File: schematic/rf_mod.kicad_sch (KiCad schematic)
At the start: 31 parts, among them J4A Conn_01x08, Q3 2N3906, Q6 2N3906, U23 4066

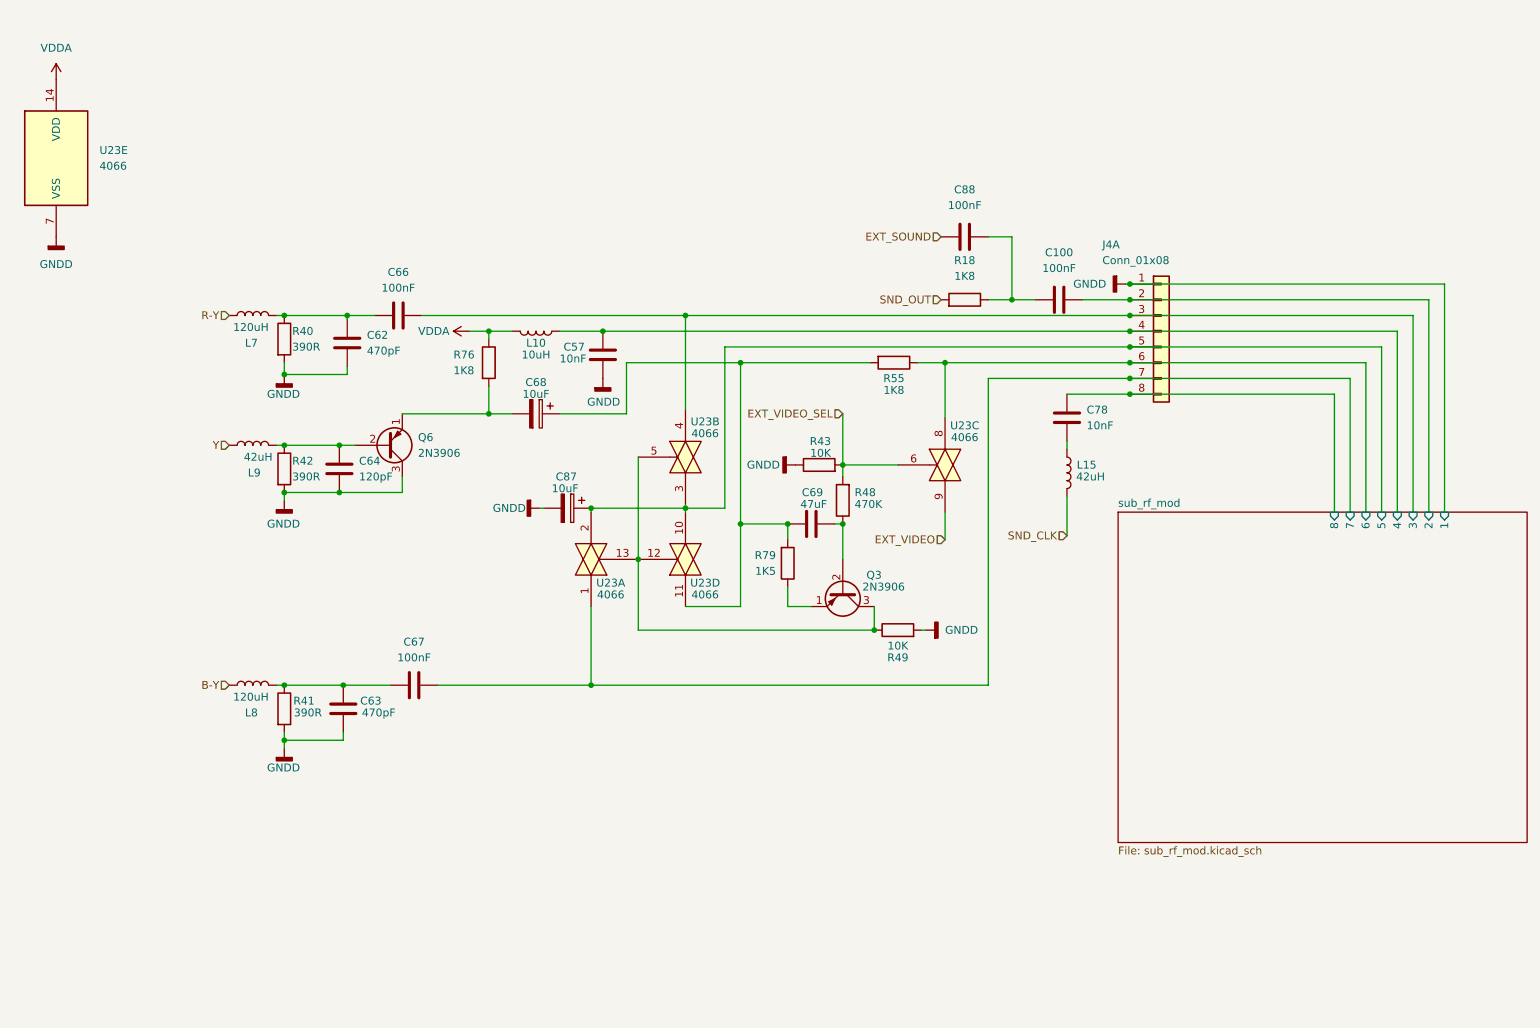
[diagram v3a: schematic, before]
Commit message: adjusted size of the sheets. added pcb version to the rev field. F.0... the 0 is for future fixes on my end. RF PCB is E.0.
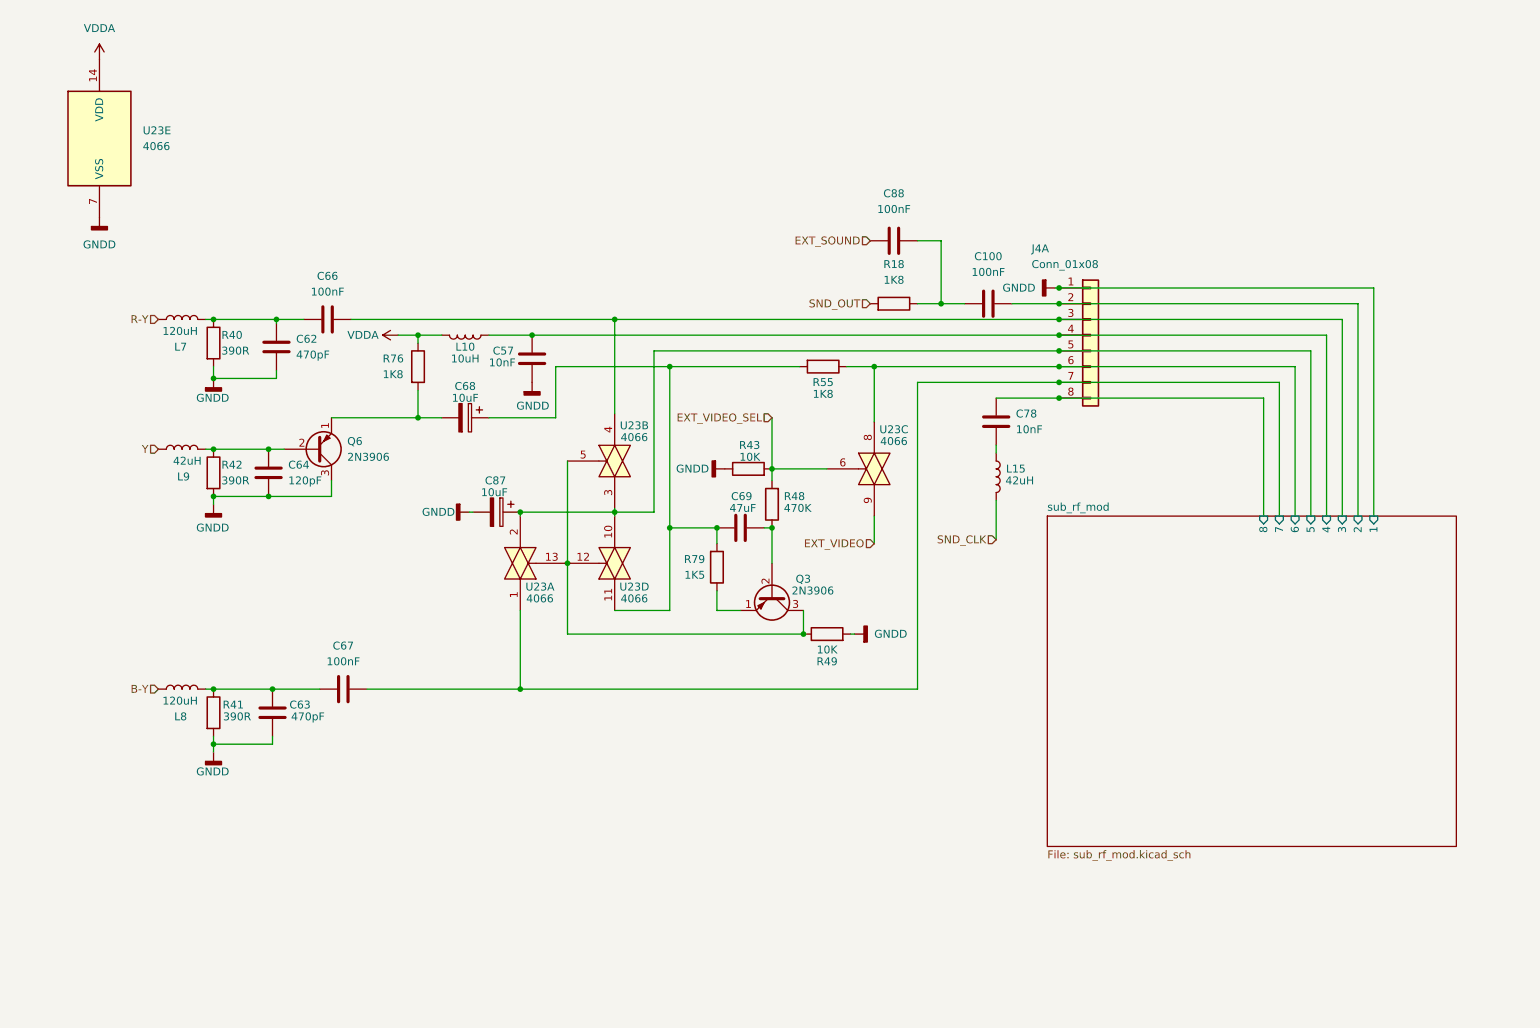
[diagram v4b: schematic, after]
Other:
- title: (none) -> Colecovision Schematic
- moved on the sheet: C100, C57, C62, C63, C64, C66, C67, C68, C69, C78, C87, C88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

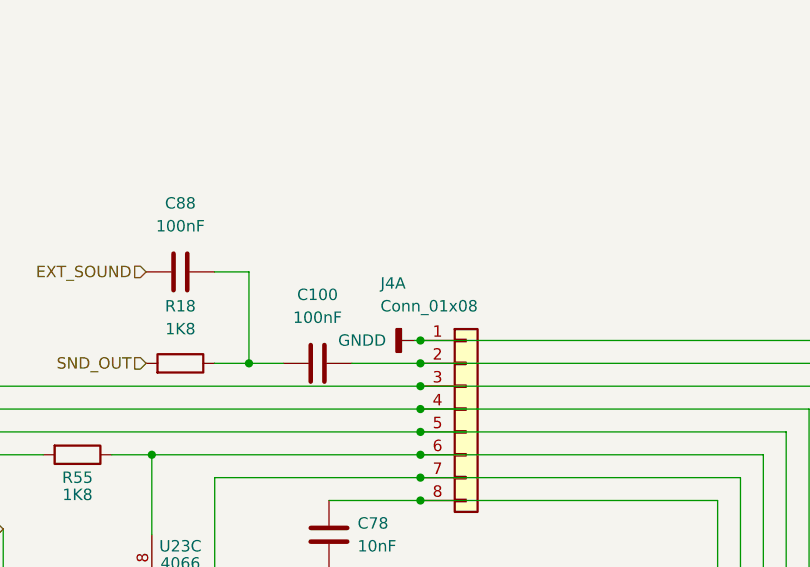
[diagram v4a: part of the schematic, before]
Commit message: cleanup, and started associating components
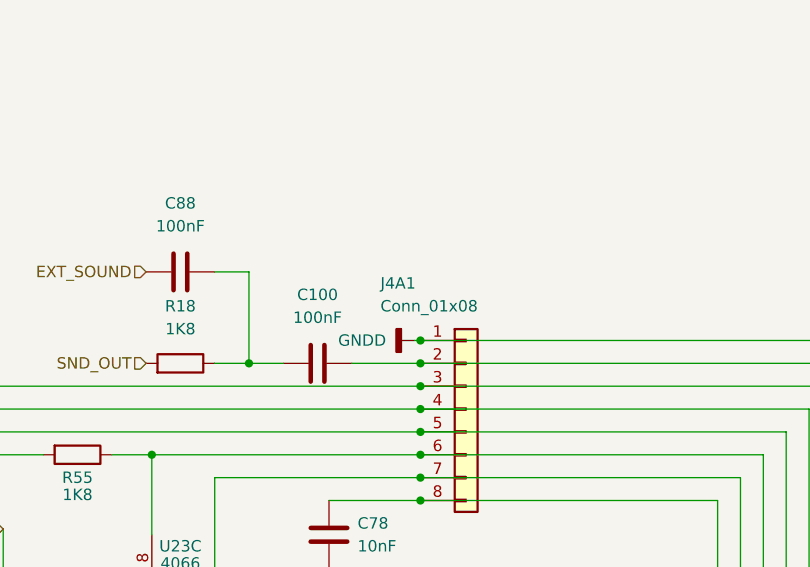
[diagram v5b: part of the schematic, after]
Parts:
- C100, C57, C66, C67, C78, C88: footprint (none) -> Capacitor_THT:C_Disc_D10.0mm_W2.5mm_P5.00mm
- C62, C63, C64: footprint (none) -> Capacitor_THT:C_Disc_D7.0mm_W2.5mm_P5.00mm
- C68, C69, C87: footprint (none) -> Capacitor_THT:CP_Radial_D5.0mm_P2.00mm
- J4A1: renamed from J4A; footprint (none) -> Connector_PinHeader_2.54mm:PinHeader_1x08_P2.54mm_Vertical
- L10, L15, L7, L8, L9: footprint (none) -> Inductor_THT:L_Axial_L12.8mm_D5.8mm_P7.62mm_Vertical_Fastron_HBCC
- Q3, Q6: footprint Package_TO_SOT_THT:TO-92_Inline -> Package_TO_SOT_THT:TO-92_Wide
- R18, R40, R41, R42, R43, R48, R49, R55, R76, R79: footprint (none) -> Resistor_THT:R_Axial_DIN0207_L6.3mm_D2.5mm_P7.62mm_Horizontal
- U23: footprint (none) -> Package_DIP:DIP-14_W7.62mm_LongPads

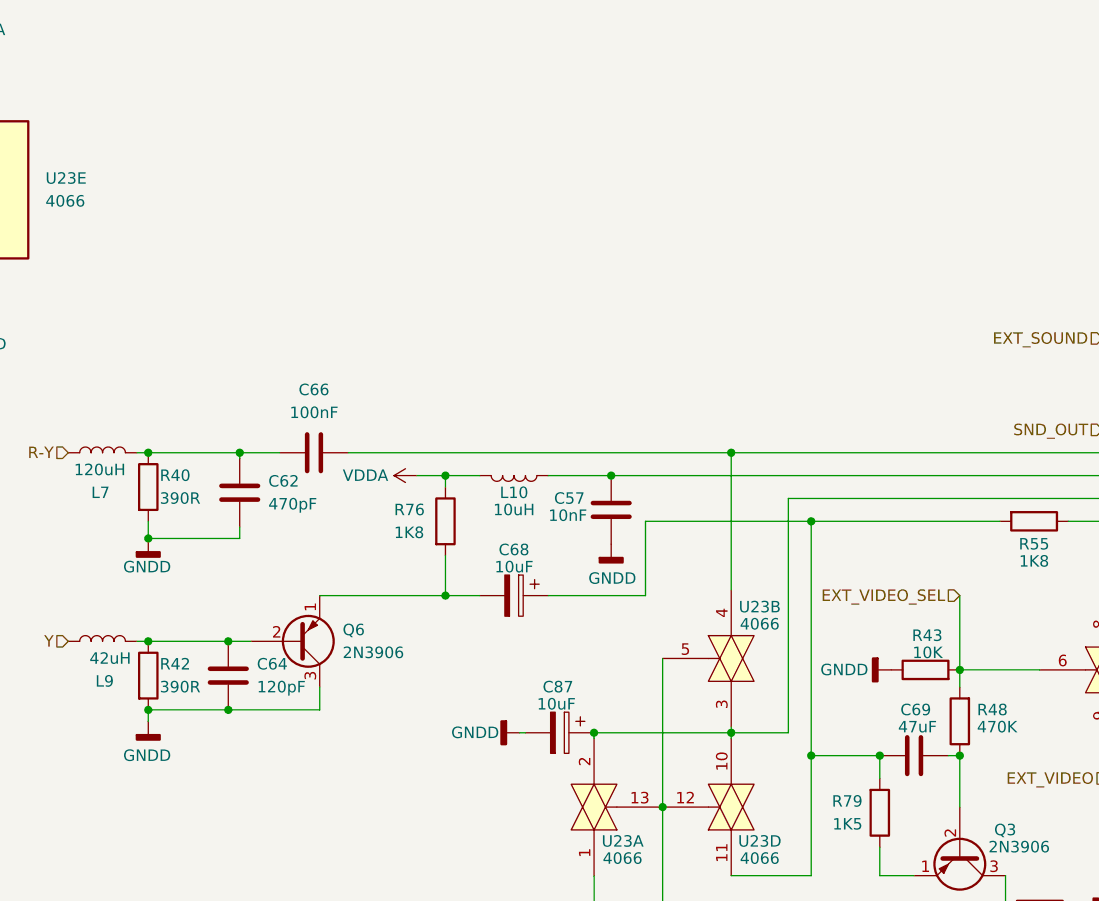
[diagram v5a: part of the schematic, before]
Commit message: first draft of board with components added, no traces
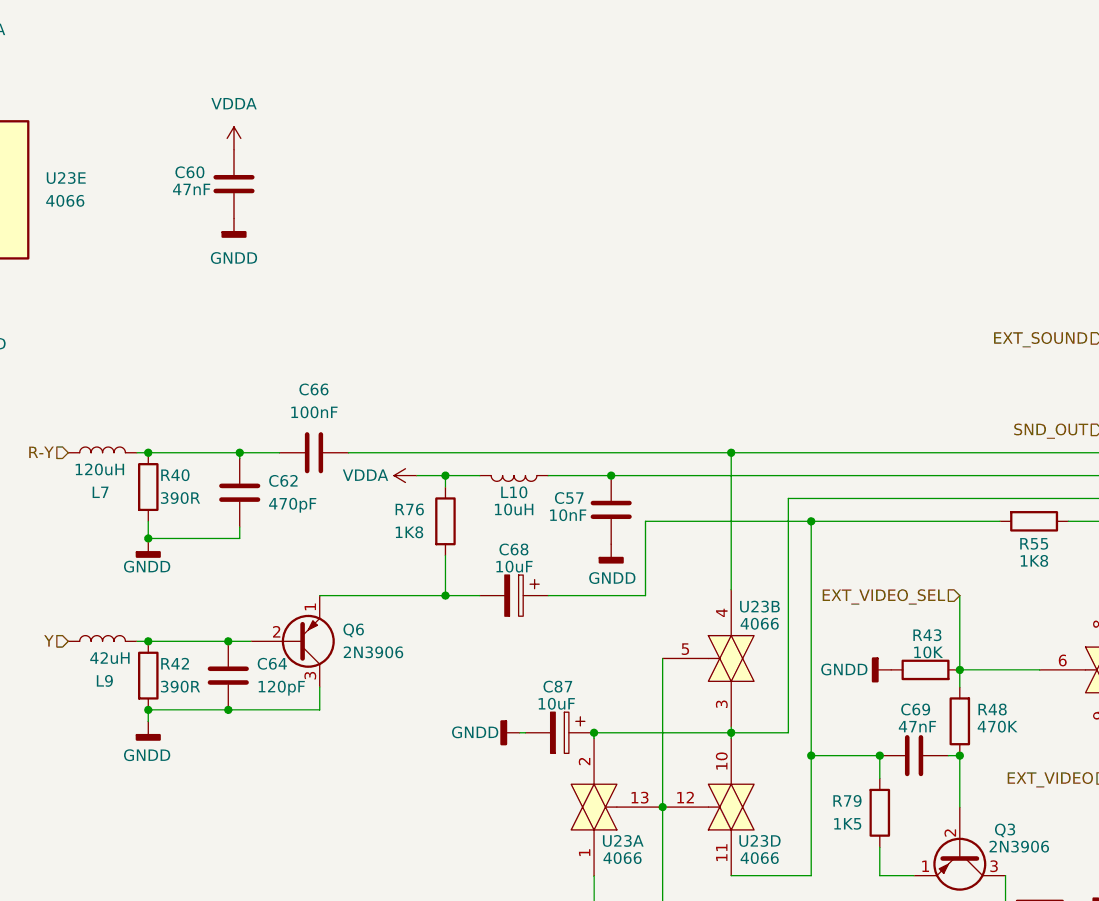
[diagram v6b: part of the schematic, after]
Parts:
- added C60: 47nF, Capacitor_THT:C_Disc_D7.0mm_W2.5mm_P5.00mm, symbol Device:C
- C100, C57, C66, C67, C78, C88: footprint Capacitor_THT:C_Disc_D10.0mm_W2.5mm_P5.00mm -> Capacitor_THT:C_Disc_D7.0mm_W2.5mm_P5.00mm
- C68, C87: footprint Capacitor_THT:CP_Radial_D5.0mm_P2.00mm -> Capacitor_THT:CP_Radial_D5.0mm_P2.50mm
- C69: value 47uF -> 47nF; footprint Capacitor_THT:CP_Radial_D5.0mm_P2.00mm -> Capacitor_THT:C_Disc_D7.0mm_W2.5mm_P5.00mm
- L10, L15, L7, L8, L9: footprint Inductor_THT:L_Axial_L12.8mm_D5.8mm_P7.62mm_Vertical_Fastron_HBCC -> Inductor_THT:L_Axial_L11.0mm_D4.5mm_P7.62mm_Vertical_Fastron_MECC
- R18, R40, R41, R42, R43, R48, R49, R55, R76, R79: footprint Resistor_THT:R_Axial_DIN0207_L6.3mm_D2.5mm_P7.62mm_Horizontal -> Resistor_THT:R_Axial_DIN0207_L6.3mm_D2.5mm_P10.16mm_Horizontal
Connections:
- net GNDD: now also C60.2
- net VDDA: now also C60.1

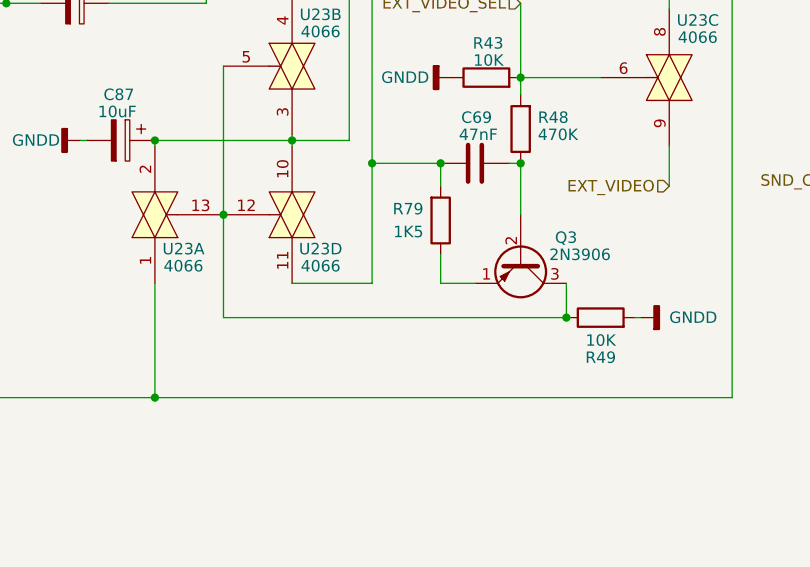
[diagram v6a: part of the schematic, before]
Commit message: added addr decode and 4066 circuit
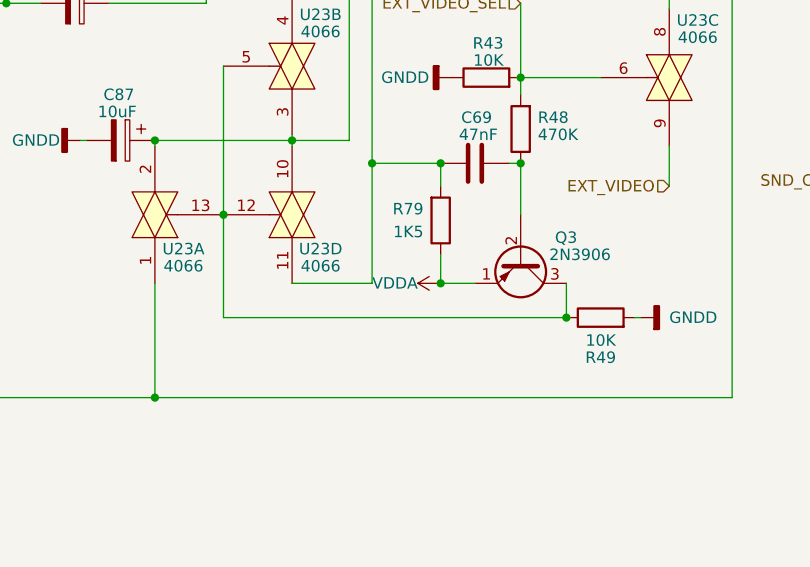
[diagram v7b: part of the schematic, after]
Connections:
- net VDDA: now also Q3.1 (E), R79.1
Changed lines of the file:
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@@
   (junction (at 194.31 66.04) (diameter 0) (color 0 0 0 0)
+  )
+  (junction (at 139.065 113.03) (diameter 0) (color 0 0 0 0)
   )
   (junction (at 66.675 86.995) (diameter 0) (color 0 0 0 0)
@@
     (pin "2")
   )
+  (symbol (lib_id "power:VDDA") (at 139.065 113.03 90) (unit 1)
+    (in_bom yes) (on_board yes)
+    (property "Reference" "#PWR?" (id 0) (at 142.875 113.03 0)
+      (effects (font (size 1.27 1.27)) hide)
+    )
+    (property "Value" "VDDA" (id 1) (at 136.525 113.03 90)
+      (effects (font (size 1.27 1.27)) (justify left))
+    )
+    (property "Footprint" "" (id 2) (at 139.065 113.03 0)
+      (effects (font (size 1.27 1.27)) hide)
+    )
+    (property "Datasheet" "" (id 3) (at 139.065 113.03 0)
+      (effects (font (size 1.27 1.27)) hide)
+    )
+    (pin "1")
+  )
   (sheet (at 192.405 97.79) (size 66.04 53.34) (fields_autoplaced)
